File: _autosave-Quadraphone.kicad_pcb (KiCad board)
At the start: 4 copper layers, 60 x 100 mm, 177 parts, among them J1 Conn_01x10_Male, J2 Conn_01x10_Male, J3 Conn_01x10_Male, J4 Conn_01x10_Male, J5 Eurorack_10_pin_power, U1 AMS1117-5.0, U10 TL072, U11 4066, U12 SSI2131, U13 TL072, U14 LM4040DBZ-2.5, U15 4066, U16 TL072, U17 SSI2131, U18 TL072, U22 SSI2131, U3 MCP6002, U4 LM4040DBZ-5, U5 MCP6004, U6 4066, U7 4066, U8 4066, U9 SSI2131

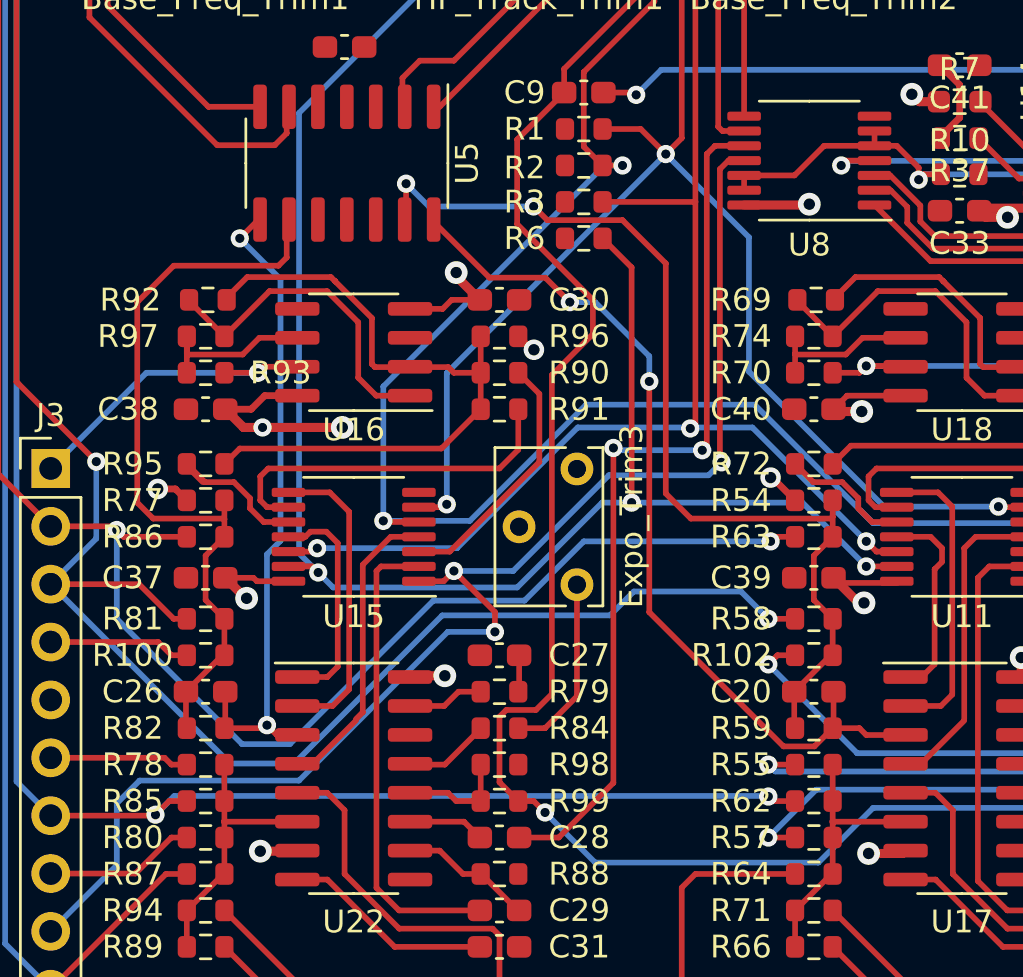
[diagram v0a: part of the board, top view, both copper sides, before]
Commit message: Routed 2.5V Power Supply
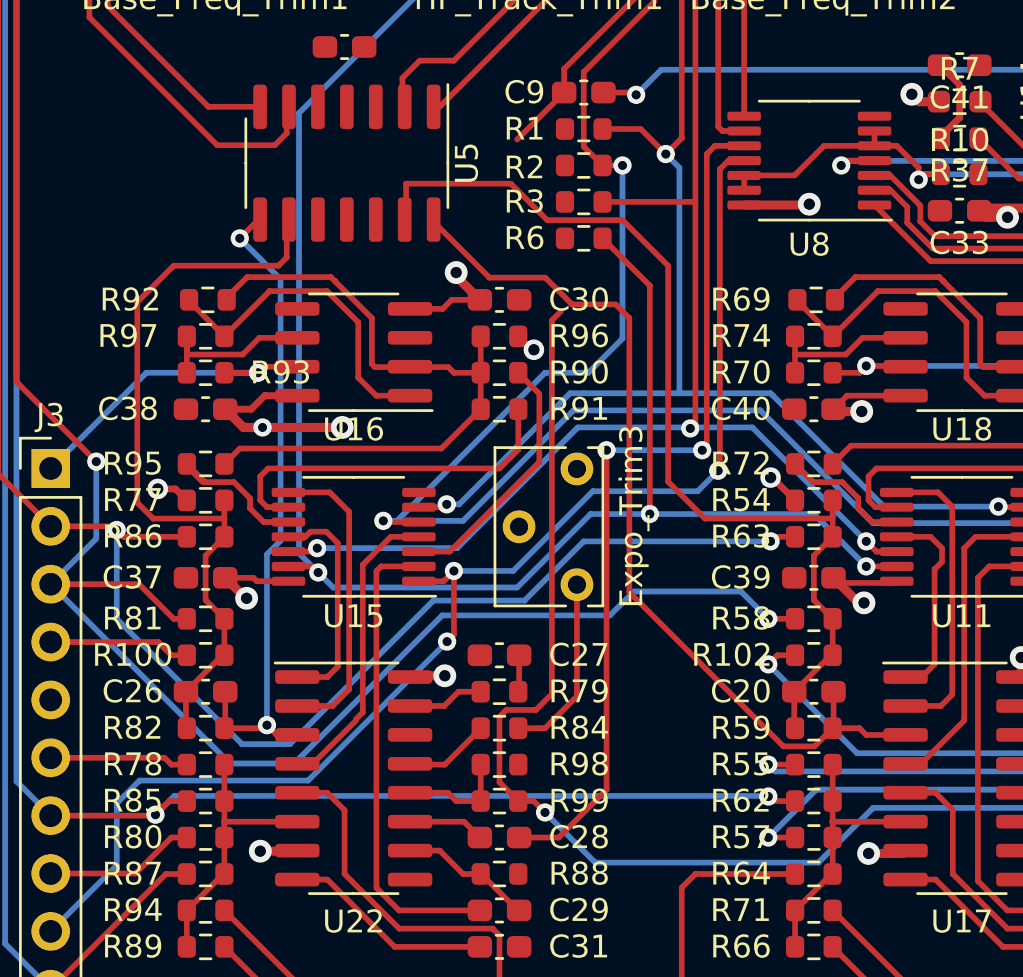
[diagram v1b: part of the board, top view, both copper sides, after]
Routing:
- net /Linear_Frequency: track 116.2 -> 106.7 mm
- net /PULSE_SW: track 127.2 -> 122.5 mm
- net /SYNCH_SIGNAL3: track 59.5 -> 57.1 mm
- net /TRIANGLE_SW: track 136.9 -> 137.6 mm
- net -5V: track 224.5 -> 225.1 mm
- net /OSCVoice4/PWM_Control: track 39.0 -> 39.5 mm, vias 2 -> 0
- net /OSCVoice4/PWM_Opamp_Mix: track 43.8 -> 43.5 mm, vias 2 -> 0
